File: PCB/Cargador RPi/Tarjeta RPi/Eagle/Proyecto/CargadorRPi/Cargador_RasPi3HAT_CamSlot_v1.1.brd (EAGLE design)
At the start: 65 x 56 mm, 22 parts, among them J2 PIN20X2, U1 MCP3208, X2 22-23-2081

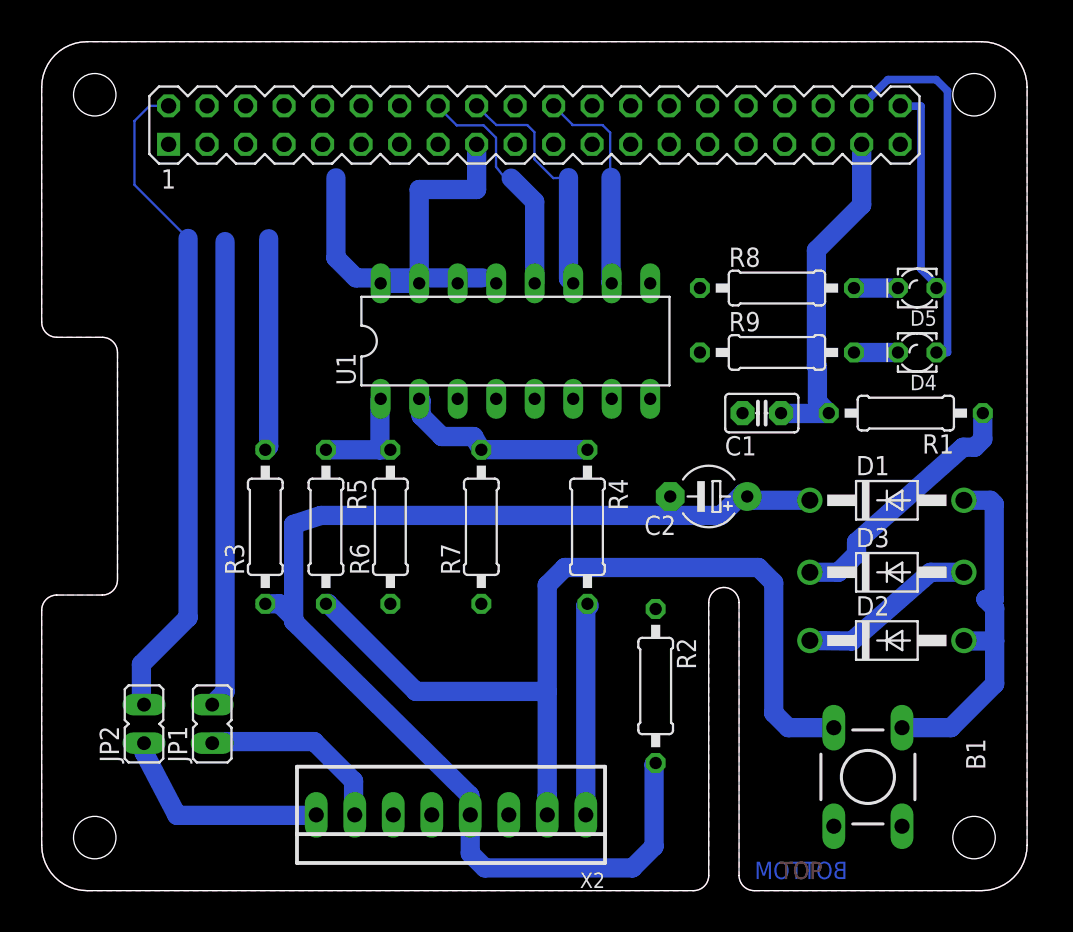
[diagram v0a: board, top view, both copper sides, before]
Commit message: Ajustes para fabricación de PCB.
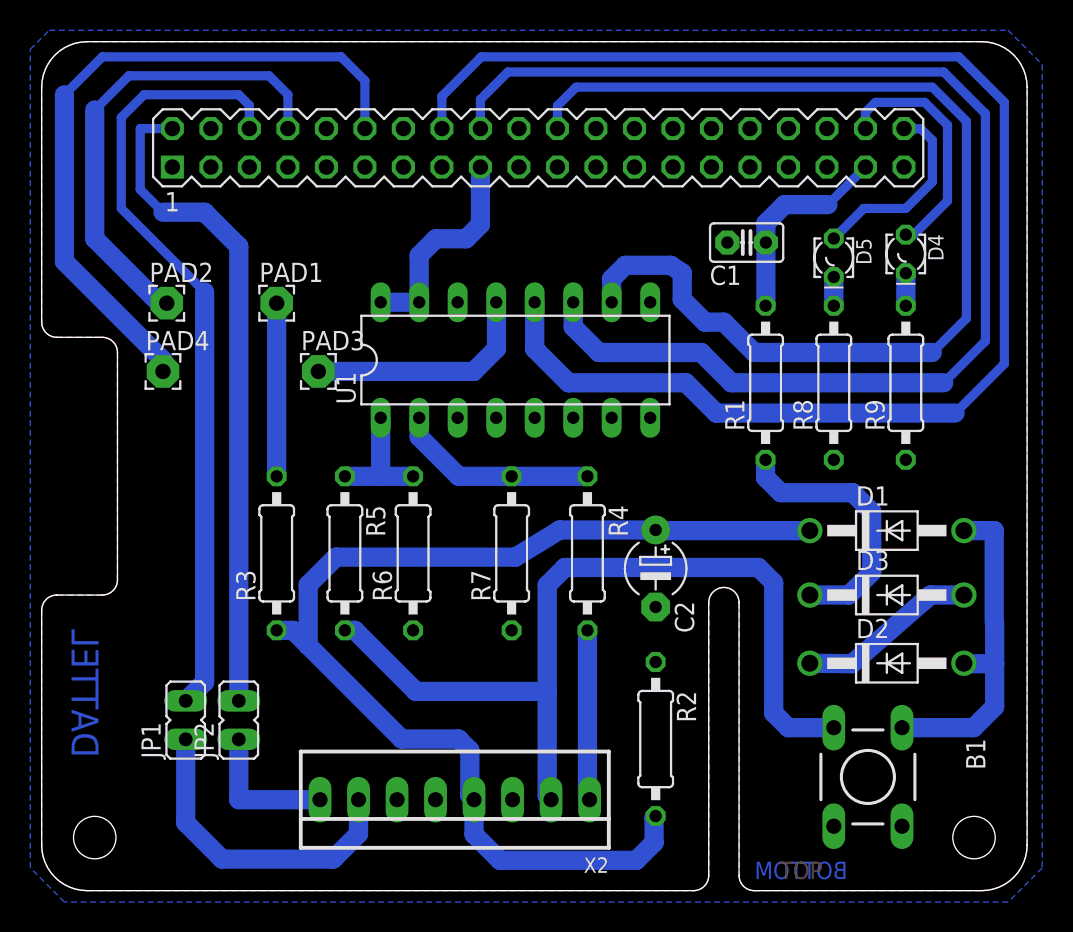
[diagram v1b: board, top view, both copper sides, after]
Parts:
- added PAD1, PAD2, PAD3, PAD4: (no value), wirepad:2,15/1,0
- moved C1 11.3 mm to (46.5, 42.8)
- moved R1 9.46 mm to (47.8, 33.5), turned to 90 degrees
- moved R9 8.73 mm to (57.0, 33.5), turned to 90 degrees
- moved R8 7.29 mm to (52.2, 33.5), turned to 90 degrees
- moved D4 6.54 mm to (57.0, 42.0), turned to 270 degrees
- moved JP2 6.25 mm to (13.0, 11.2)
- moved C2 5.90 mm to (40.5, 21.2), turned to 270 degrees
- moved D5 5.85 mm to (52.2, 41.8), turned to 270 degrees
- moved R2 3.50 mm to (40.5, 10.0)
- moved R7 2.66 mm to (31.0, 22.2)
- moved R6 2.30 mm to (24.5, 22.2)
- moved R5 2.15 mm to (20.0, 22.2)
- moved D1 2.00 mm to (55.8, 23.8)
- moved R3 1.90 mm to (15.5, 22.2)
- moved JP1 1.77 mm to (9.50, 11.2)
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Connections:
- removed net DGND: U1.DGND
- new net N$20: PAD3.1, U1.CLK
- new net N$8: J2.12, PAD4.1
- net GND: now also U1.DGND
- net N$11: now also PAD1.1, R3.2; no longer J2.12, U1.CLK
- net N$2: now also PAD2.1; no longer R3.2
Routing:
- net N$9: track 15.6 -> 96.0 mm
- net N$10: track 16.2 -> 83.6 mm
- net N$21: track 14.7 -> 72.5 mm
- net N$8: track 0.00 -> 45.6 mm
- net N$18: track 30.9 -> 52.2 mm
- net N$2: track 14.0 -> 31.4 mm
- net N$20: track 0.00 -> 15.4 mm
- net N$1: track 22.5 -> 13.6 mm
- net N$6: track 24.7 -> 16.0 mm
- net N$17: track 12.7 -> 20.8 mm
- net N$26: track 82.4 -> 74.9 mm
- net N$11: track 16.7 -> 11.4 mm
- net N$19: track 14.5 -> 9.34 mm
- net N$15: track 14.3 -> 11.2 mm
- net N$16: track 61.0 -> 58.1 mm
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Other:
- board text added: "DATTEL"
